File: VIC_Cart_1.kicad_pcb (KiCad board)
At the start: 2 copper layers, 126.5 x 77.3 mm, 30 parts, among them J1 VIC-20 Expansion Port, J2 I2C Display, U1 ATMEGA328P-PU, U2 KM681000CLG-5L, U3 M27C160, U4 74LS148, U5 74LS21, U6 74LS21, U7 74LS32, U8 74LS32, U9 74LS32, Y1 16MHz

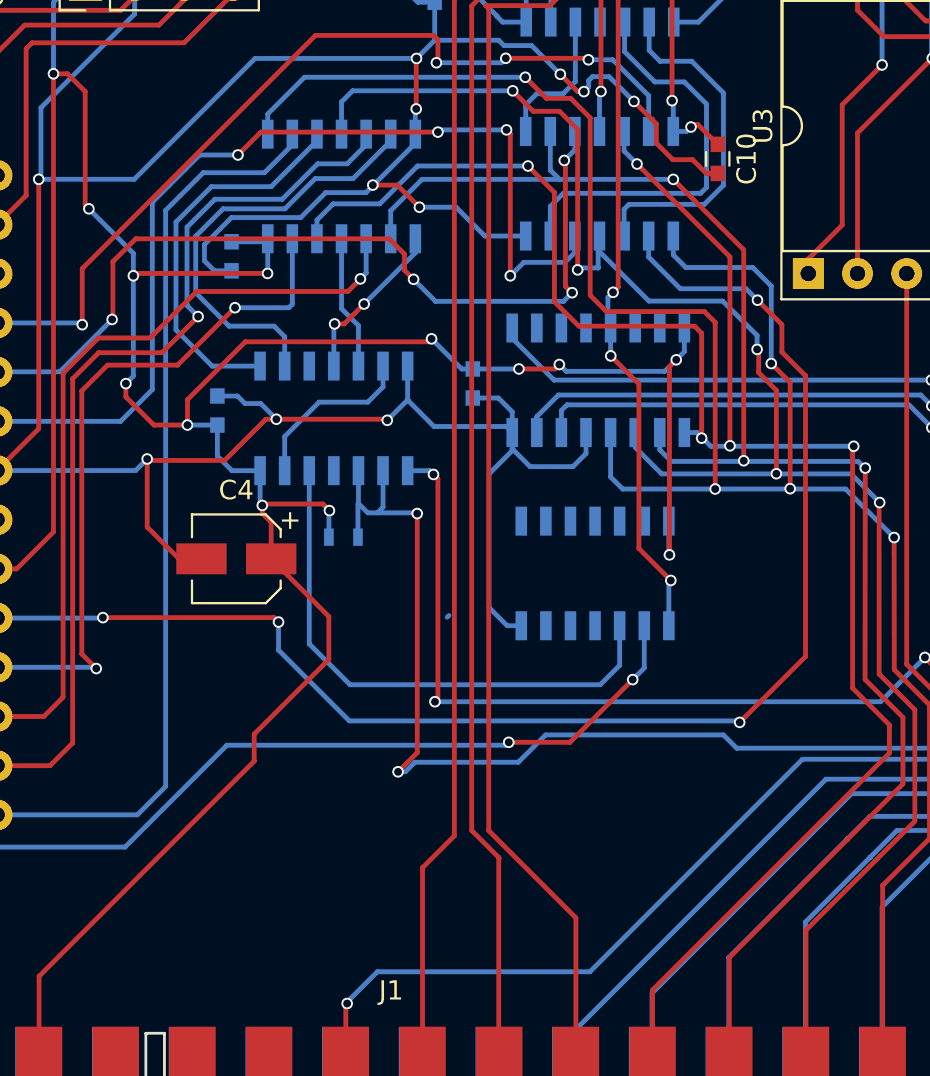
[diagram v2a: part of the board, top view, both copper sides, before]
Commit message: Added Footprint library to project Added explanatory text to PCB
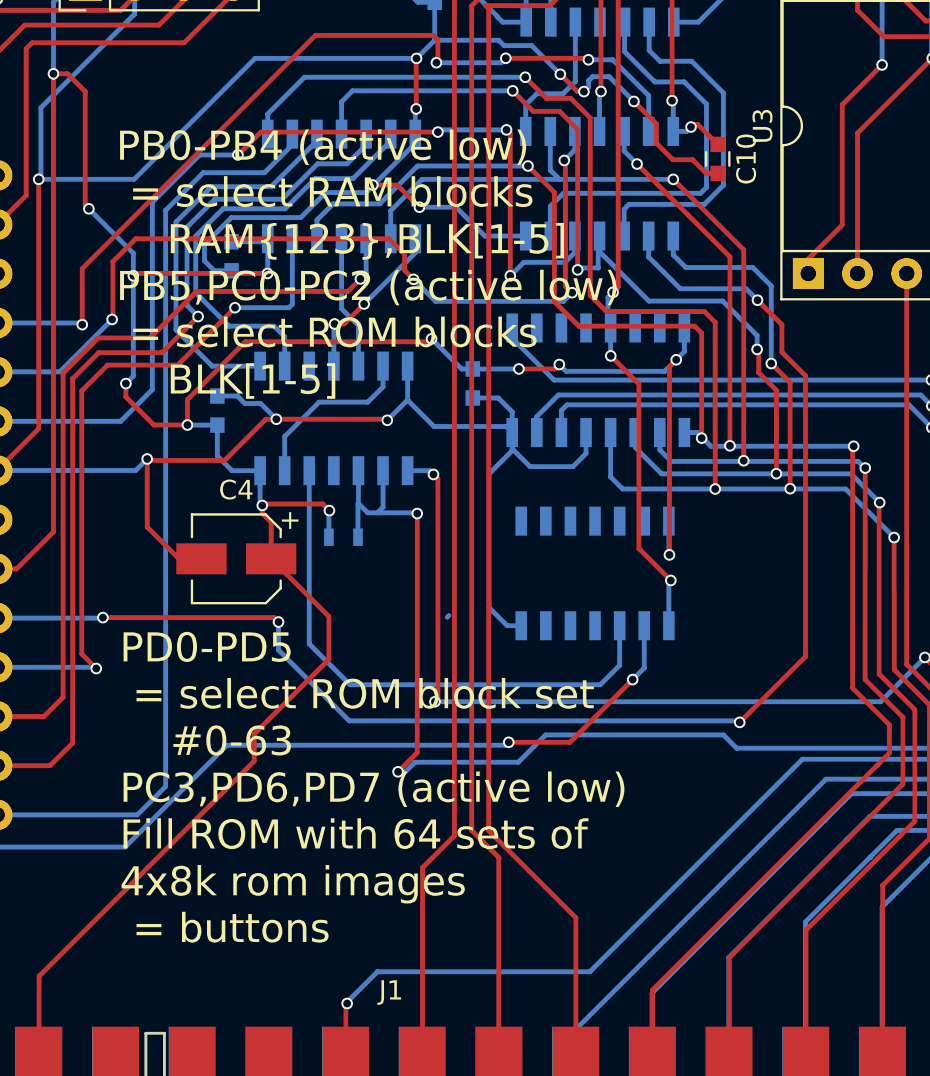
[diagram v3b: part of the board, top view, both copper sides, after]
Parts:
- J1: value VIC-20 Expansion Port -> VIC-20_Expansion_Port; footprint MyConnectors:VIC_EXP -> VIC_Connectors:VIC_EXP
- U2: footprint MyConnectors:SOP-32_14.12x20.87mm_Pitch1.27mm -> VIC_Connectors:SOP-32_14.12x20.87mm_Pitch1.27mm
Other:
- board text added: "PB0-PB4 (active low) = select RAM blocks RAM{123},BLK[1-5] PB5,PC0-PC2 (active low) = select ROM blocks BLK[1-5]"
- board text added: "PD0-PD5 = select ROM block set #0-63 PC3,PD6,PD7 (active low) Fill ROM with 64 sets of 4x8k rom images = buttons"

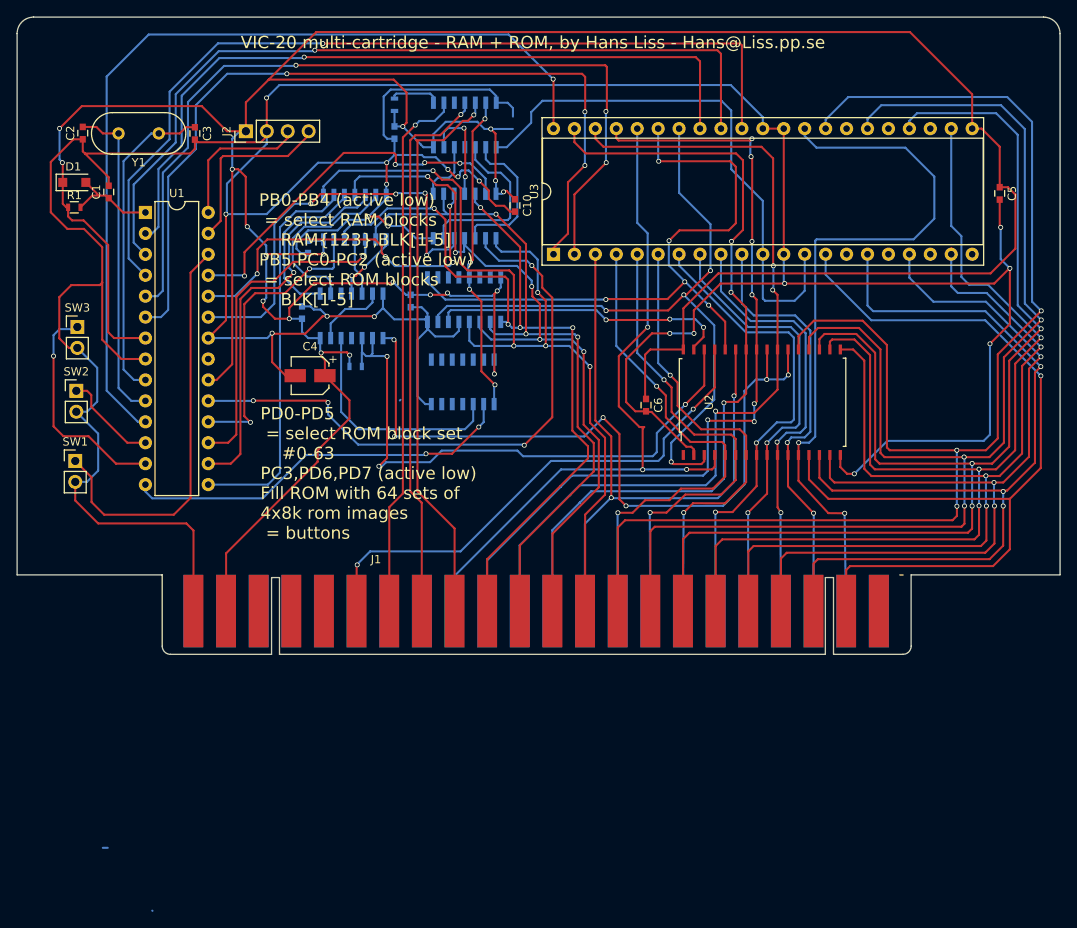
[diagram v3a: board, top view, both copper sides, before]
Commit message: Added back ground plane
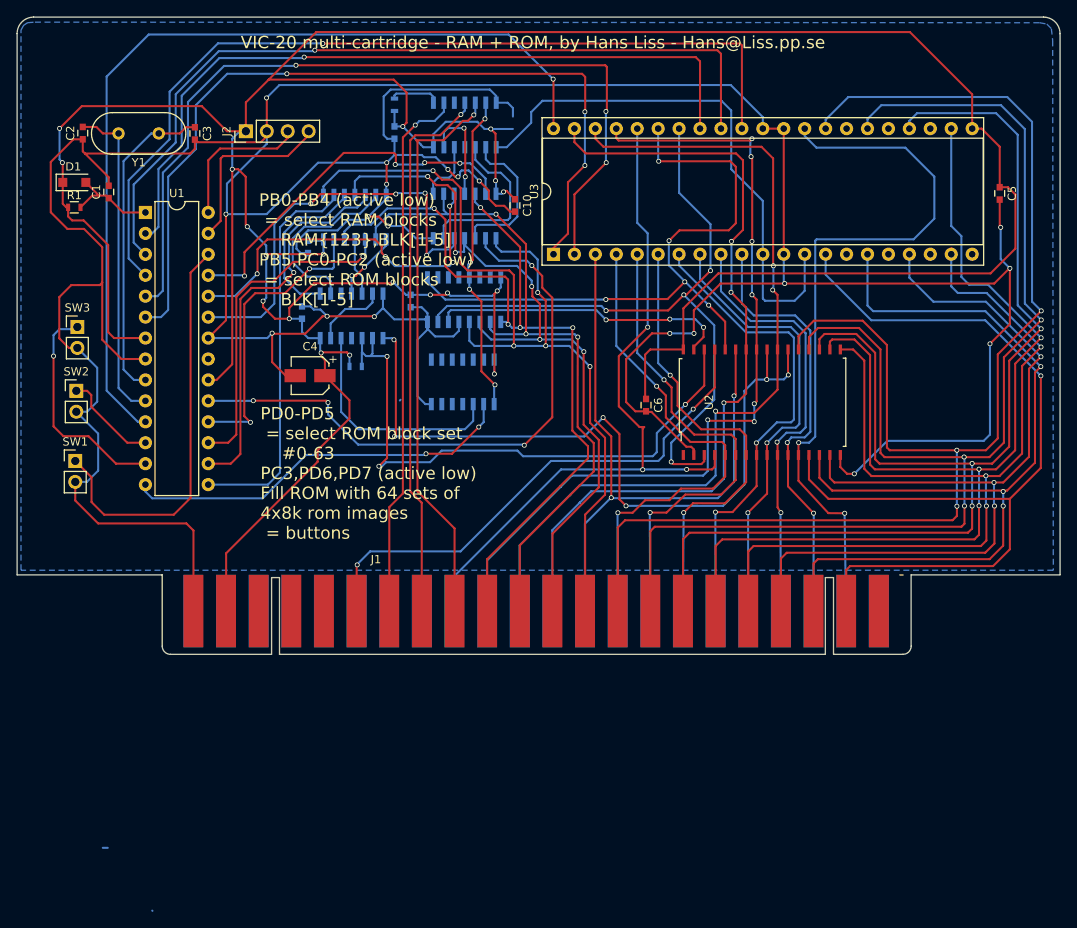
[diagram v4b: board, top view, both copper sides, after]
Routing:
- added copper zone on B.Cu, net GND
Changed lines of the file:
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@@
   (segment (start 85.4202 82.2198) (end 98.3361 82.2198) (width 0.25) (layer B.Cu) (net 72))
   (segment (start 83.312 80.1116) (end 85.4202 82.2198) (width 0.25) (layer B.Cu) (net 72))
+  (zone (net 22) (net_name GND) (layer B.Cu) (hatch edge 0.508)
+    (connect_pads (clearance 0.208))
+    (min_thickness 0.254)
+    (fill yes (arc_segments 16) (thermal_gap 0.208) (thermal_bridge_width 0.608) (smoothing chamfer))
+    (polygon
+      (pts
+        (xy 168.0591 32.89808) (xy 168.93286 33.0581) (xy 169.48658 33.61182) (xy 169.6466 35.0393) (xy 169.72534 99.32924)
+        (xy 44.47286 99.32924) (xy 44.47286 34.16808) (xy 44.47032 33.78708) (xy 44.79036 33.21558) (xy 45.26534 32.89808)
+        (xy 46.16196 32.82696)
+      )
+    )
+  )
 )

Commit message: Switched around BLK[1-5] to encoder to put ROM blocks in correct order.
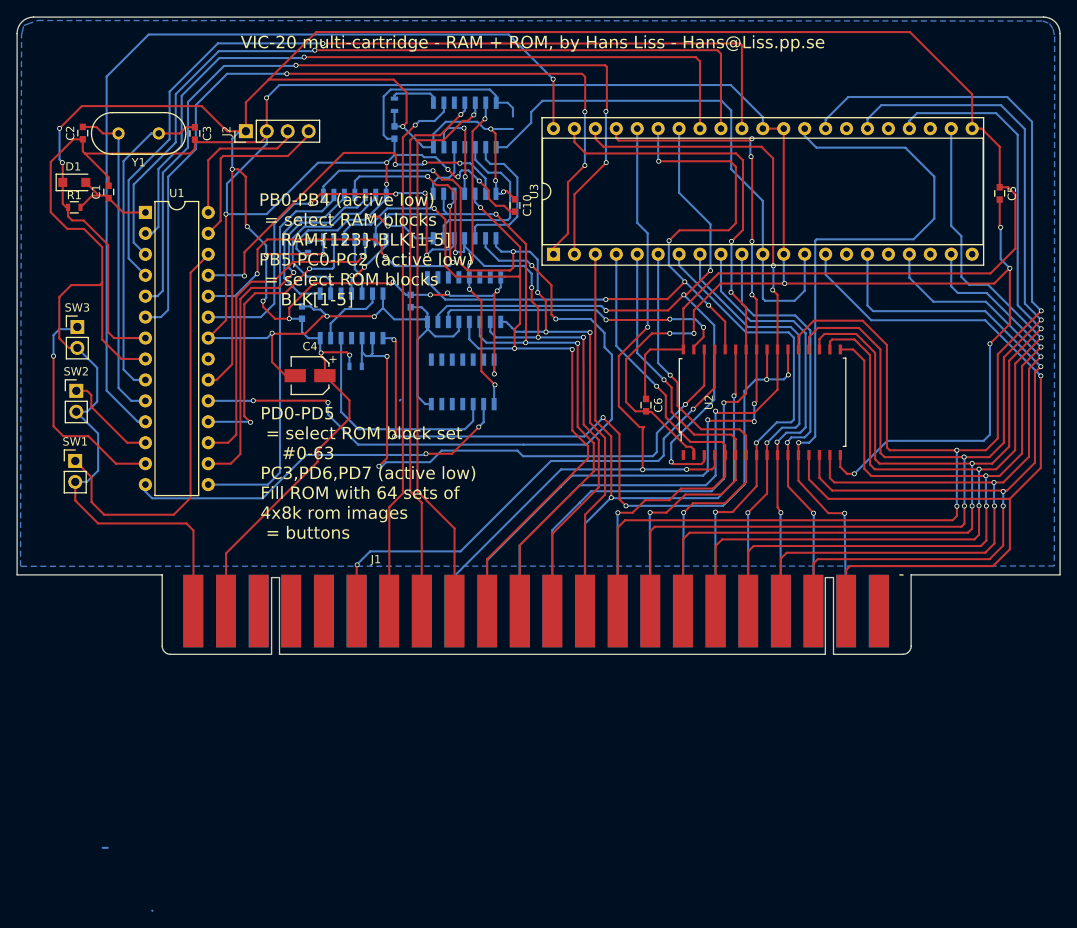
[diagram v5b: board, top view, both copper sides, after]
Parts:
- SW1, SW2, SW3: value (none) -> SW_Push
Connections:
- J1 pad 1: (no net) -> Net-(J1-Pad1)
- J1 pad 18: (no net) -> Net-(J1-Pad18)
- J1 pad 19: (no net) -> Net-(J1-Pad19)
- J1 pad 20: (no net) -> Net-(J1-Pad20)
- J1 pad A: (no net) -> Net-(J1-PadA)
- J1 pad S: (no net) -> Net-(J1-PadS)
- J1 pad T: (no net) -> Net-(J1-PadT)
- J1 pad U: (no net) -> Net-(J1-PadU)
- J1 pad V: (no net) -> Net-(J1-PadV)
- J1 pad W: (no net) -> Net-(J1-PadW)
- J1 pad X: (no net) -> Net-(J1-PadX)
- J1 pad Y: (no net) -> Net-(J1-PadY)
- J1 pad Z: (no net) -> Net-(J1-PadZ)
- U1 pad 21: (no net) -> Net-(U1-Pad21)
- U2 pad 1: (no net) -> Net-(U2-Pad1)
- U3 pad 15: (no net) -> Net-(U3-Pad15)
- U3 pad 17: (no net) -> Net-(U3-Pad17)
- U3 pad 19: (no net) -> Net-(U3-Pad19)
- U3 pad 21: (no net) -> Net-(U3-Pad21)
- U3 pad 24: (no net) -> Net-(U3-Pad24)
- U3 pad 26: (no net) -> Net-(U3-Pad26)
- U3 pad 28: (no net) -> Net-(U3-Pad28)
- U4 pad 1: /~BLK5 -> /~BLK1
- U4 pad 10: (no net) -> Net-(U4-Pad10)
- U4 pad 11: (no net) -> Net-(U4-Pad11)
- U4 pad 12: (no net) -> Net-(U4-Pad12)
- U4 pad 14: (no net) -> Net-(U4-Pad14)
- U4 pad 15: (no net) -> Net-(U4-Pad15)
- U4 pad 2: /~BLK3 -> /~BLK2
- U4 pad 3: /~BLK2 -> /~BLK3
- U4 pad 4: /~BLK1 -> /~BLK5
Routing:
- net /~SEL_ROM_BLK1: track 73.4 -> 86.2 mm
- net /~BLK1: track 111.4 -> 100.2 mm
- net /~BLK3: track 85.2 -> 87.7 mm
- net /~BLK5: track 102.2 -> 104.3 mm, vias 5 -> 4

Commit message: Minor change
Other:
- board text added: "PD0-PD5 = select ROM block set #0-63 PC3,PD6,PD7 (active low) = buttons Fill ROM with 64 sets of 4x8k rom images"
- board text removed: "PD0-PD5 = select ROM block set #0-63 PC3,PD6,PD7 (active low) Fill ROM with 64 sets of 4x8k rom images = buttons"
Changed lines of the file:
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@@
     (links 162)
     (no_connects 0)
-    (area 43.924999 32.139799 170.615001 109.604881)
+    (area 43.924999 32.139799 170.615001 140.982582)
     (thickness 1.6)
     (drawings 23)
@@
     )
   )
-  (gr_text "PD0-PD5\n = select ROM block set\n    #0-63\nPC3,PD6,PD7 (active low)\nFill ROM with 64 sets of\n4x8k rom images\n = buttons\n" (at 73.5203 87.5665) (layer F.SilkS)
+  (gr_text "PD0-PD5\n = select ROM block set\n    #0-63\nPC3,PD6,PD7 (active low)\n = buttons\nFill ROM with 64 sets of\n4x8k rom images\n" (at 73.5203 87.5665) (layer F.SilkS)
     (effects (font (size 1.5 1.5) (thickness 0.3)) (justify left))
   )
